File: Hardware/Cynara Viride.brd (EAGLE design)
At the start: 160 x 100 mm, 168 parts, among them Q1 TXC-7B, Q2 TXC-7WNEO, SW1 430181038816, SW2 , T1 PDTC143, T2 PDTC143, T3 PDTC143, T4 PDTC143, T5 PDTC143, U1 TM4C129EN, U2 MCP1826S 3V3, U3 LM4132 3V3, U4 XC6SLX9-3TQG, U5 M25P16-SO8, U6 MCP1826S 1V2, X1 EDGE 50p, X11 SOCK2X17, X12 SOCK2X17, X13 SOCK2X17, X2 EDGE 50p, X23 debug xilinx, X24 debug 10p, X3 EDGE 50p, X4 EDGE 50p, X5 MicroMatch 24, X6 , X7 SOCK2X17, X8 RJ45-LAN-10/100

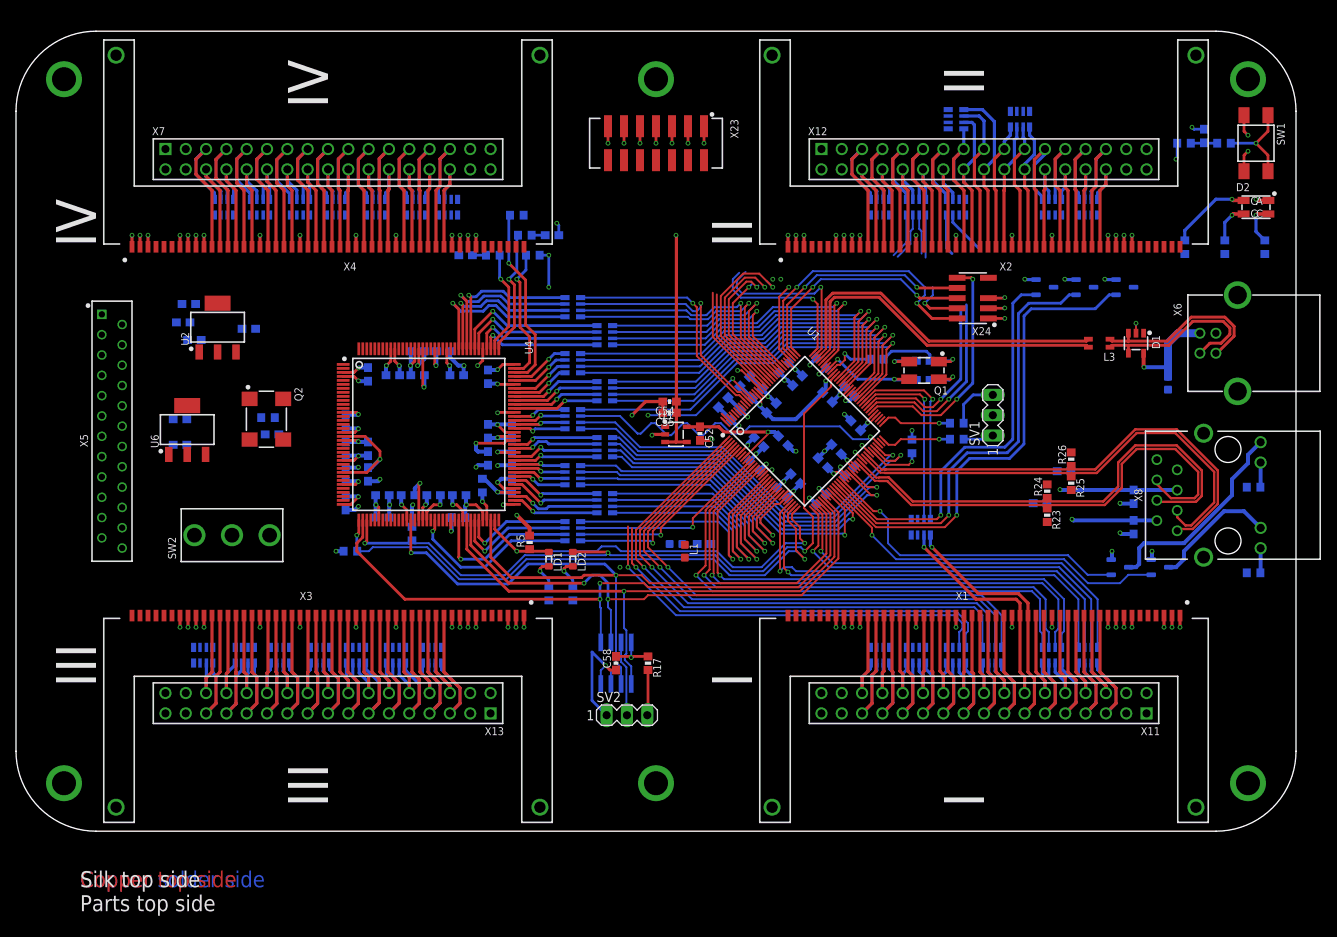
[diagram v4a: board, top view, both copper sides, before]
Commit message: All Petals are connected in the layout.
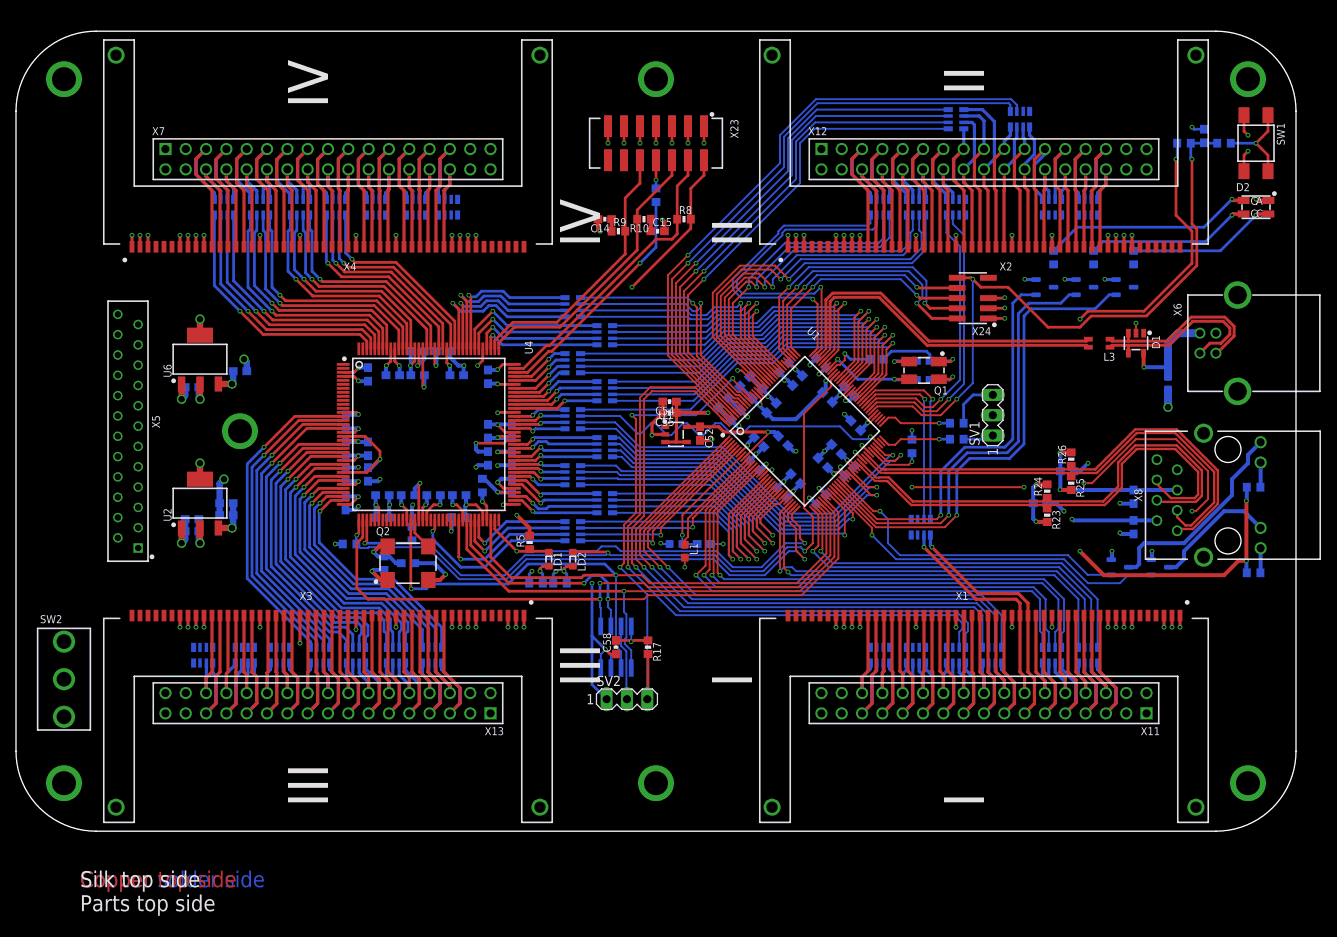
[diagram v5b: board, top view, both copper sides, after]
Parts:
- moved C17 28.4 mm to (22.0, 37.5), turned to 180 degrees
- moved SW2 27.7 mm to (6.00, 19.0), turned to 0 degrees
- moved Q2 25.2 mm to (49.0, 33.5), turned to 0 degrees
- moved C18 24.7 mm to (26.3, 39.5)
- moved C59 23.4 mm to (49.0, 33.5)
- moved R18 23.3 mm to (46.0, 33.5), turned to 90 degrees
- moved C56 22.4 mm to (22.0, 39.0), turned to 180 degrees
- moved U2 22.1 mm to (23.0, 41.0)
- moved C57 22.0 mm to (26.3, 41.0)
- moved R8 19.4 mm to (83.5, 76.5), flipped to the top, turned to 0 degrees
- moved C14 18.0 mm to (73.6, 76.5), flipped to the top, turned to 180 degrees
- moved R11 17.6 mm to (80.0, 79.5), turned to 90 degrees
- moved R19 16.5 mm to (139.7, 71.7)
- moved R20 16.5 mm to (129.7, 71.7)
- moved R21 16.5 mm to (134.7, 71.7)
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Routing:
- net 5V_USB: track 0.00 -> 214.9 mm, vias 0 -> 1
- net +3.3V: track 167.5 -> 283.4 mm, vias 37 -> 49
- net MCU_II_P: track 0.00 -> 77.0 mm, vias 0 -> 1
- net GND: track 241.4 -> 316.7 mm, vias 113 -> 128
- net MCU_II_O: track 0.00 -> 74.8 mm, vias 0 -> 1
- net MCU_II_N: track 0.00 -> 64.8 mm, vias 0 -> 1
- net MCU_II_M: track 0.00 -> 63.5 mm, vias 0 -> 1
- net MCU_II_L: track 0.00 -> 62.3 mm, vias 0 -> 1
- net MCU_II_K: track 0.00 -> 60.9 mm, vias 0 -> 1
- net !RST: track 33.3 -> 82.6 mm, vias 2 -> 3
- net FPGA_III_P: track 0.00 -> 40.7 mm, vias 0 -> 1
- net PJ1_FLASHWP: track 21.6 -> 61.5 mm
- net FPGA_III_O: track 0.00 -> 39.7 mm, vias 0 -> 1
- net FPGA_III_N: track 0.00 -> 38.7 mm, vias 0 -> 1
- net FPGA_III_M: track 0.00 -> 37.8 mm, vias 0 -> 1
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
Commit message: Added proposal for power routing to the Petals.
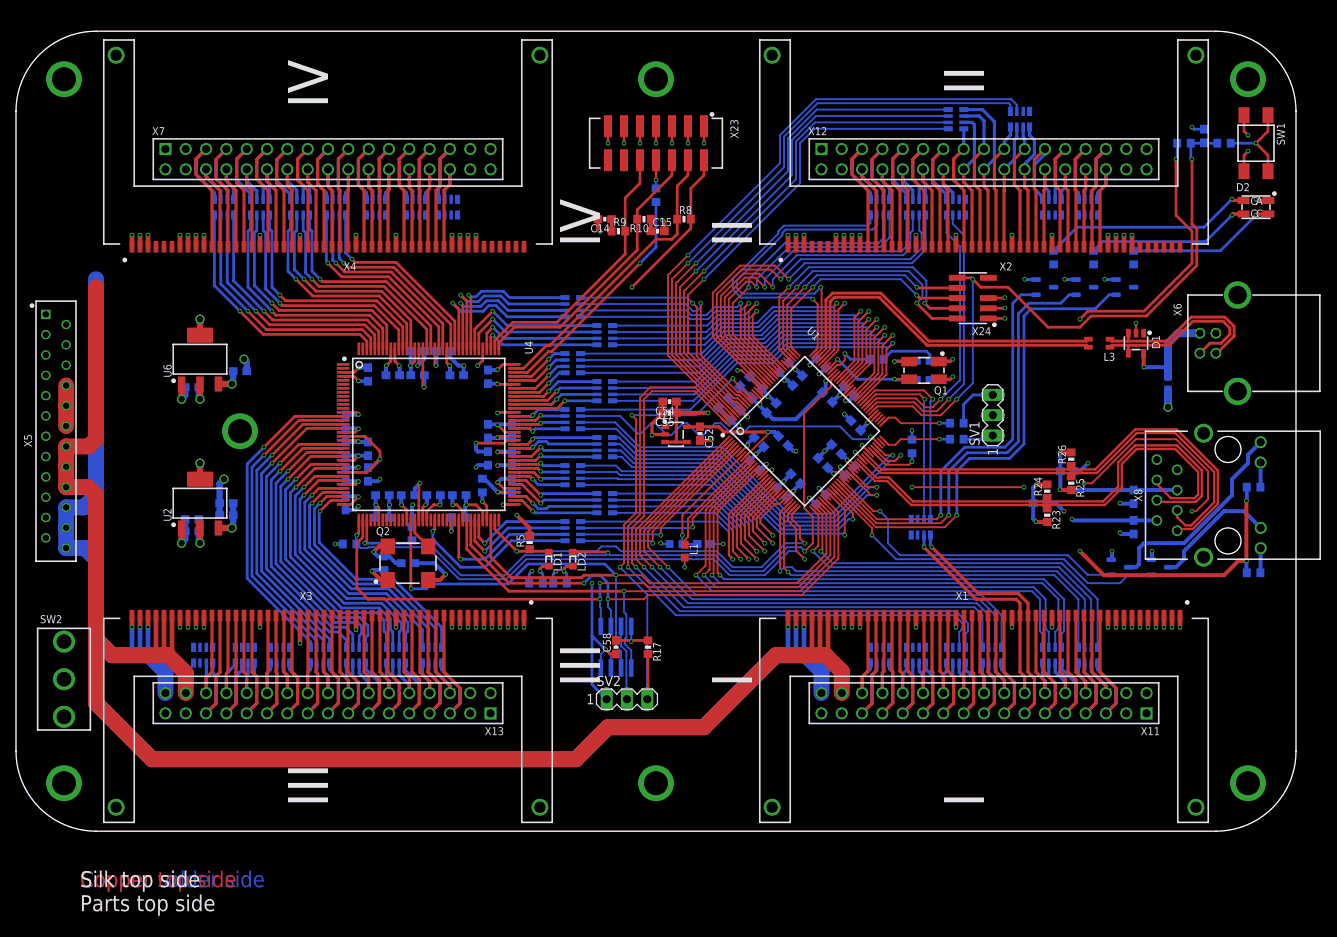
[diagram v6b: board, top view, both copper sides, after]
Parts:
- moved X5 9.00 mm to (5.00, 50.0), turned to 90 degrees
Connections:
- net +5V: now also X11.2, X12.2, X13.2, X7.2; no longer X11.1, X12.1, X13.1, X7.1
- net GND: now also X11.1, X11.3, X11.31, X11.33, X12.1, X12.3, X12.31, X12.33, X13.1, X13.3, X13.31, X13.33, X7.1, X7.3, X7.31, X7.33; no longer X11.2, X11.32, X11.34, X11.4, X12.2, X12.32, X12.34, X12.4, X13.2, X13.32, X13.34, X13.4, X7.2, X7.32, X7.34, X7.4
- net VEXT_A: now also X11.32, X12.32, X13.32, X7.32; no longer X11.31, X12.31, X13.31, X7.31
- net VEXT_B: now also X11.34, X12.34, X13.34, X7.34; no longer X11.33, X12.33, X13.33, X7.33
- net X3V3: now also X11.4, X12.4, X13.4, X7.4; no longer X11.3, X12.3, X13.3, X7.3
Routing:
- net X3V3: track 19.3 -> 259.3 mm, vias 0 -> 6
- net VEXT_B: track 15.6 -> 204.4 mm, vias 0 -> 6
- net VEXT_A: track 26.9 -> 209.0 mm
- net X5V: track 36.1 -> 5.08 mm

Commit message: Completed routing for the power rails.
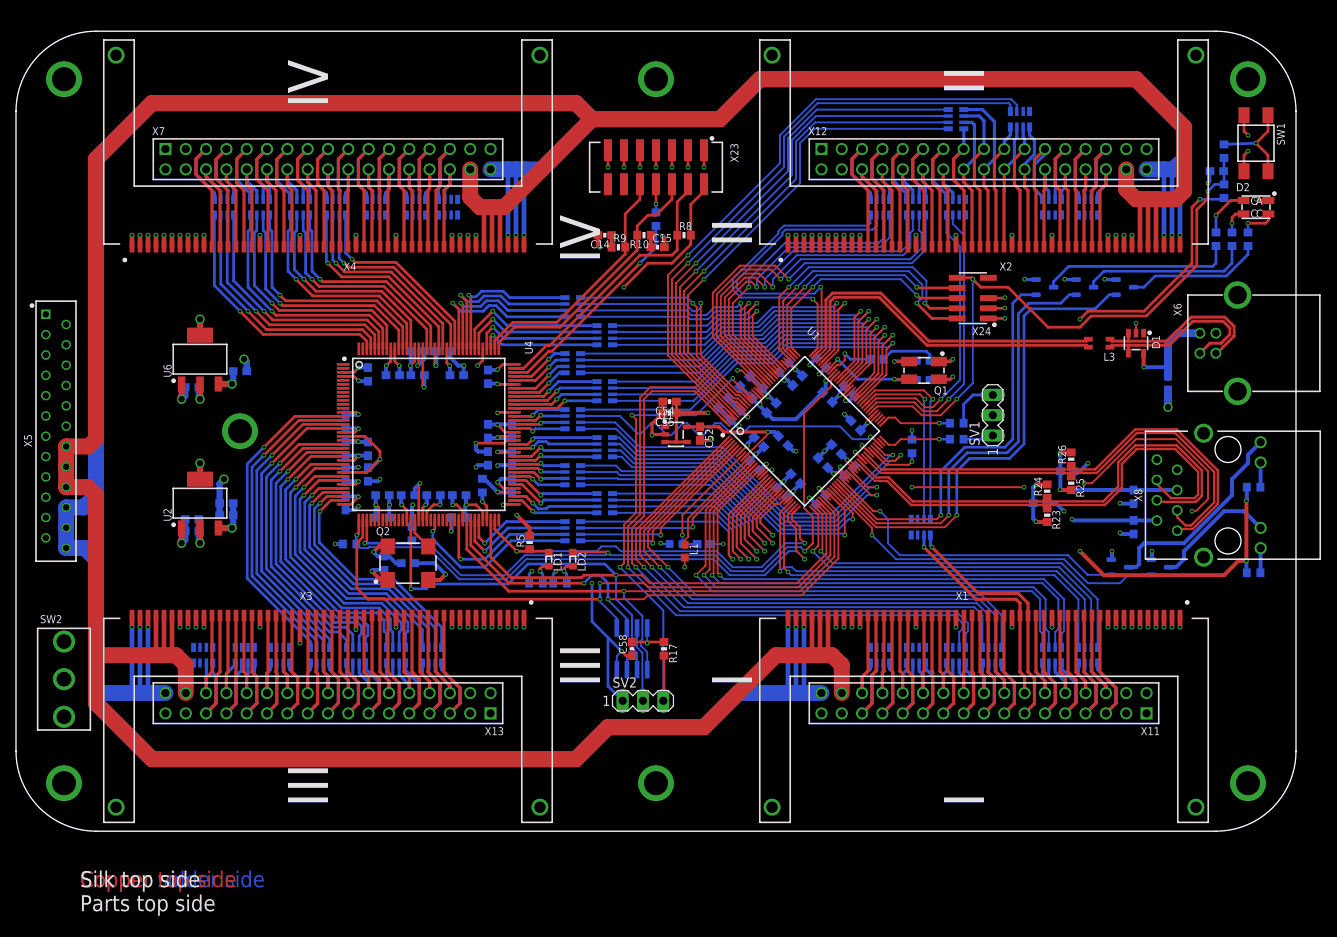
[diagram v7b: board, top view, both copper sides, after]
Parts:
- moved R20 20.4 mm to (150.0, 74.0)
- moved R21 17.5 mm to (152.0, 74.0)
- moved R19 14.5 mm to (154.0, 74.0)
- moved R13 7.81 mm to (151.0, 80.0), turned to 270 degrees
- moved C51 4.68 mm to (150.1, 82.5), turned to 0 degrees
- moved R11 3.00 mm to (80.0, 76.5)
- moved X23 3.00 mm to (80.0, 83.0)
- moved C58 2.01 mm to (77.0, 22.8)
- moved R17 2.01 mm to (81.0, 22.8)
- moved SV2 2.01 mm to (78.4, 16.3)
- moved U5 2.01 mm to (77.0, 22.8)
- moved C14 2.00 mm to (73.6, 74.5)
- moved C15 2.00 mm to (80.2, 73.0)
- moved R10 2.00 mm to (78.5, 74.5)
- moved R8 2.00 mm to (83.5, 74.5)
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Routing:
- net VEXT_B: track 204.4 -> 465.0 mm, vias 6 -> 12
- net VEXT_A: track 209.0 -> 444.2 mm
- net X3V3: track 259.3 -> 445.0 mm, vias 6 -> 12
- net X5V: track 5.08 -> 36.4 mm
- net N$77: track 0.00 -> 24.1 mm
- net N$78: track 0.00 -> 21.1 mm
- net N$13: track 26.5 -> 6.37 mm
- net N$75: track 20.7 -> 3.49 mm
- net N$76: track 0.00 -> 17.0 mm
- net N$12: track 18.8 -> 4.64 mm
- net +3.3V: track 283.4 -> 279.2 mm
- net !RST: track 82.6 -> 79.2 mm
- net FPGA_TDO: track 29.8 -> 26.8 mm
- net FPGA_TDI: track 34.3 -> 31.3 mm
- net FPGA_TCK: track 35.9 -> 33.5 mm
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
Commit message: Added VBUS detect circuitry. Drill size of mounting holes is 3.5 mm to fit M3 bolts.
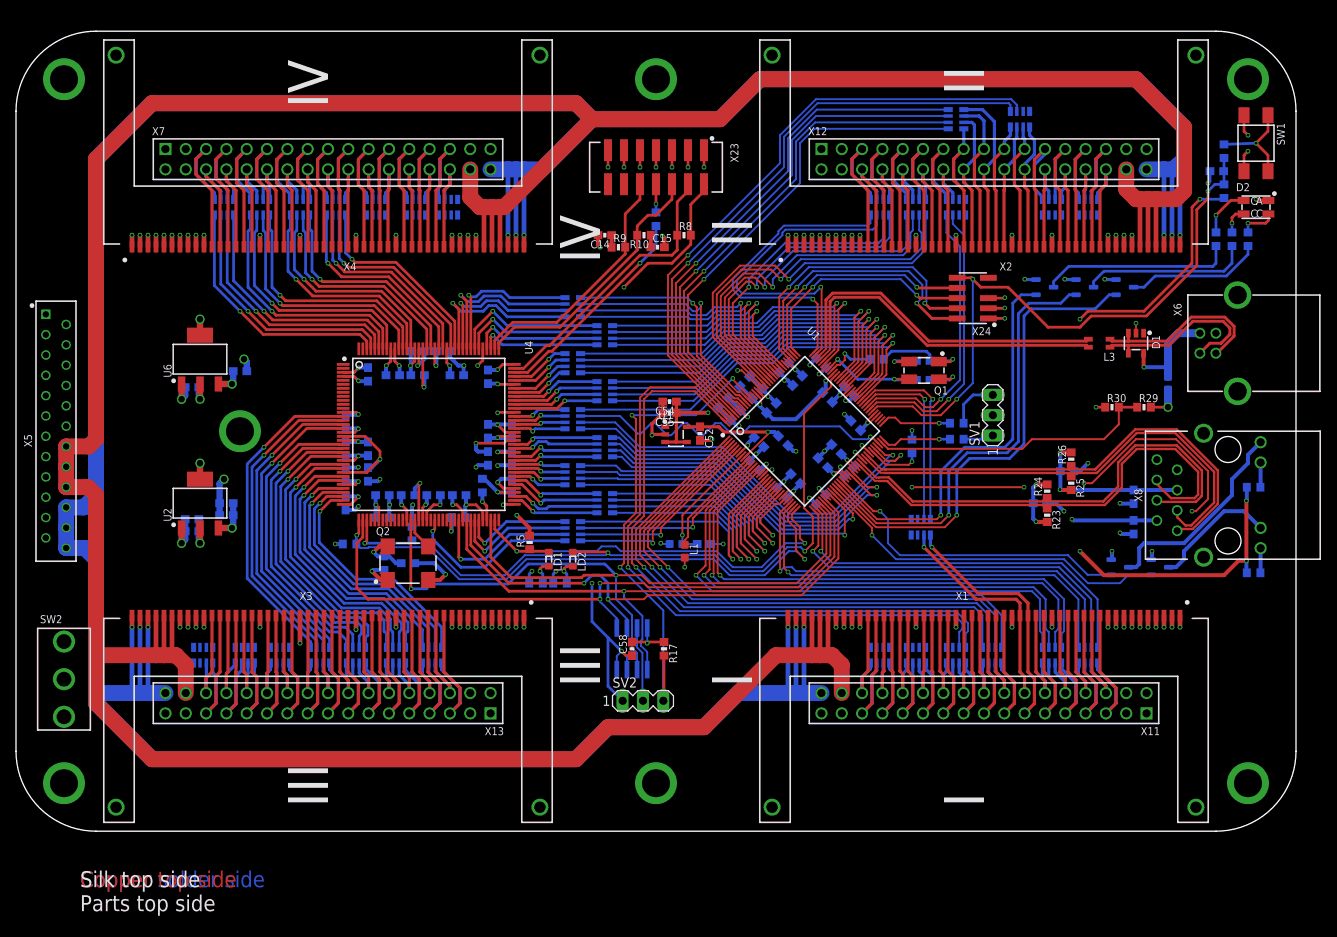
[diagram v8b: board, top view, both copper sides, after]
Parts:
- added R29: 5.6K, Cynara-Passives:R0603
- added R30: 10K, Cynara-Passives:R0603
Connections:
- removed net USB_DETECT1: U1.102
- removed net USB_DETECT2: U1.63
- new net USB_DETECT: R29.1, R30.2, U1.63
- net 5V_USB: now also R29.2
- net GND: now also R30.1
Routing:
- net USB_DETECT: track 0.00 -> 35.8 mm
- net 5V_USB: track 214.9 -> 217.1 mm
- net GND: track 316.7 -> 317.9 mm, vias 128 -> 129
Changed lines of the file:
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@@
 <attribute name="ORDERCODE" value="61400416121" x="152.7" y="61" size="1.778" layer="27" rot="R270" display="off"/>
 </element>
+<element name="R29" library="Cynara-Passives" package="R0603" value="5.6K" x="141" y="53"/>
+<element name="R30" library="Cynara-Passives" package="R0603" value="10K" x="137" y="53"/>
 </elements>
 <signals>
@@
 <wire x1="75" y1="29" x2="75" y2="32" width="0.25" layer="16"/>
 </signal>
-<signal name="USB_DETECT1">
-<contactref element="U1" pad="102"/>
+<signal name="USB_DETECT">
+<contactref element="R29" pad="1"/>
+<contactref element="R30" pad="2"/>
+<contactref element="U1" pad="63"/>
+<wire x1="140.15" y1="53" x2="137.85" y2="53" width="0.35" layer="1"/>
+<wire x1="137.85" y1="53" x2="137.85" y2="50.85" width="0.25" layer="1"/>
+<wire x1="137.85" y1="50.85" x2="136" y2="49" width="0.25" layer="1"/>
+<wire x1="136" y1="49" x2="127" y2="49" width="0.25" layer="1"/>
+<wire x1="127" y1="49" x2="125.8" y2="47.8" width="0.25" layer="1"/>
+<wire x1="125.8" y1="47.8" x2="109.0024375" y2="47.8" width="0.25" layer="1"/>
+<wire x1="109.0024375" y1="47.8" x2="108.145940625" y2="48.656496875" width="0.25" layer="1"/>
 </signal>
 <signal name="RUPT3">
@@
 <contactref element="X13" pad="31"/>
 <contactref element="X13" pad="33"/>
+<contactref element="R30" pad="1"/>
+<wire x1="136.15" y1="53" x2="135" y2="53" width="0.35" layer="1"/>
+<via x="135" y="53" extent="1-16" drill="0.35"/>
 <wire x1="102.5001" y1="26.9522" x2="102.5" y2="26.95" width="0" layer="19" extent="1-1"/>
 </signal>
@@
 </signal>
 <signal name="N$15">
-<via x="6" y="94" extent="1-16" drill="3"/>
-<via x="28" y="50" extent="1-16" drill="3"/>
-<wire x1="28" y1="50" x2="6" y2="94" width="0" layer="19" extent="1-1"/>
+<via x="6" y="94" extent="1-16" drill="3.5"/>
 </signal>
 <signal name="N$16">
-<via x="6" y="6" extent="1-16" drill="3"/>
+<via x="6" y="6" extent="1-16" drill="3.5"/>
 </signal>
 <signal name="N$17">
-<via x="154" y="6" extent="1-16" drill="3"/>
+<via x="154" y="6" extent="1-16" drill="3.5"/>
 </signal>
 <signal name="N$19">
-<via x="80" y="6" extent="1-16" drill="3"/>
+<via x="80" y="6" extent="1-16" drill="3.5"/>
 </signal>
 <signal name="N$20">
-<via x="80" y="94" extent="1-16" drill="3"/>
-<via x="154" y="94" extent="1-16" drill="3"/>
-<wire x1="80" y1="94" x2="154" y2="94" width="0" layer="19" extent="1-1"/>
+<via x="80" y="94" extent="1-16" drill="3.5"/>
 </signal>
 <signal name="OLED_MOSI">
@@
 <wire x1="72" y1="6" x2="14.3" y2="6" width="1" layer="15"/>
 <wire x1="14.3" y1="6" x2="6" y2="14.3" width="1" layer="15"/>
-</signal>
-<signal name="USB_DETECT2">
-<contactref element="U1" pad="63"/>
+<contactref element="R29" pad="2"/>
+<wire x1="141.85" y1="53" x2="144" y2="53" width="0.35" layer="1"/>
 </signal>
 <signal name="FREE">
@@
 <wire x1="153.495" y1="40" x2="155.58" y2="37.915" width="0.5" layer="16"/>
 </signal>
+<signal name="N$22">
+<via x="28" y="50" extent="1-16" drill="3.5"/>
+</signal>
+<signal name="N$23">
+<via x="154" y="94" extent="1-16" drill="3.5"/>
+</signal>
 </signals>
